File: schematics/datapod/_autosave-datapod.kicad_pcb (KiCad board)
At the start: 2 copper layers, 152.7 x 152.7 mm, 61 parts, among them J1 Conn_01x02, J2 Conn_02x03_Odd_Even, J3 Conn_01x02, J4 DB9_Female, J5 DB9_Male_MountingHoles, J6 Micro_SD_Card, J7 Conn_02x02_Odd_Even, J8 Conn_01x02_Female, K1 DS2E-SL2-DC5V, K2 DS2E-SL2-DC5V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

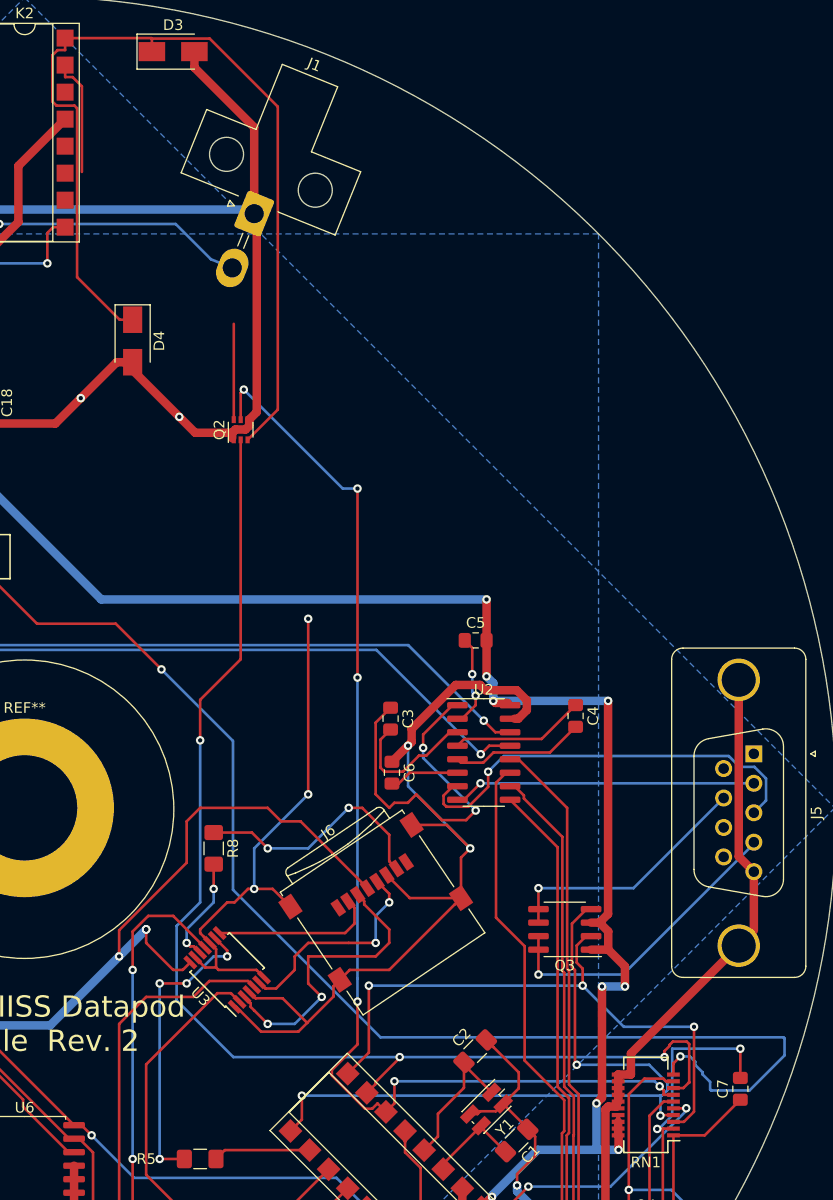
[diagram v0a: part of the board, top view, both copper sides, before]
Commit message: added 3d models that somehow were lost.
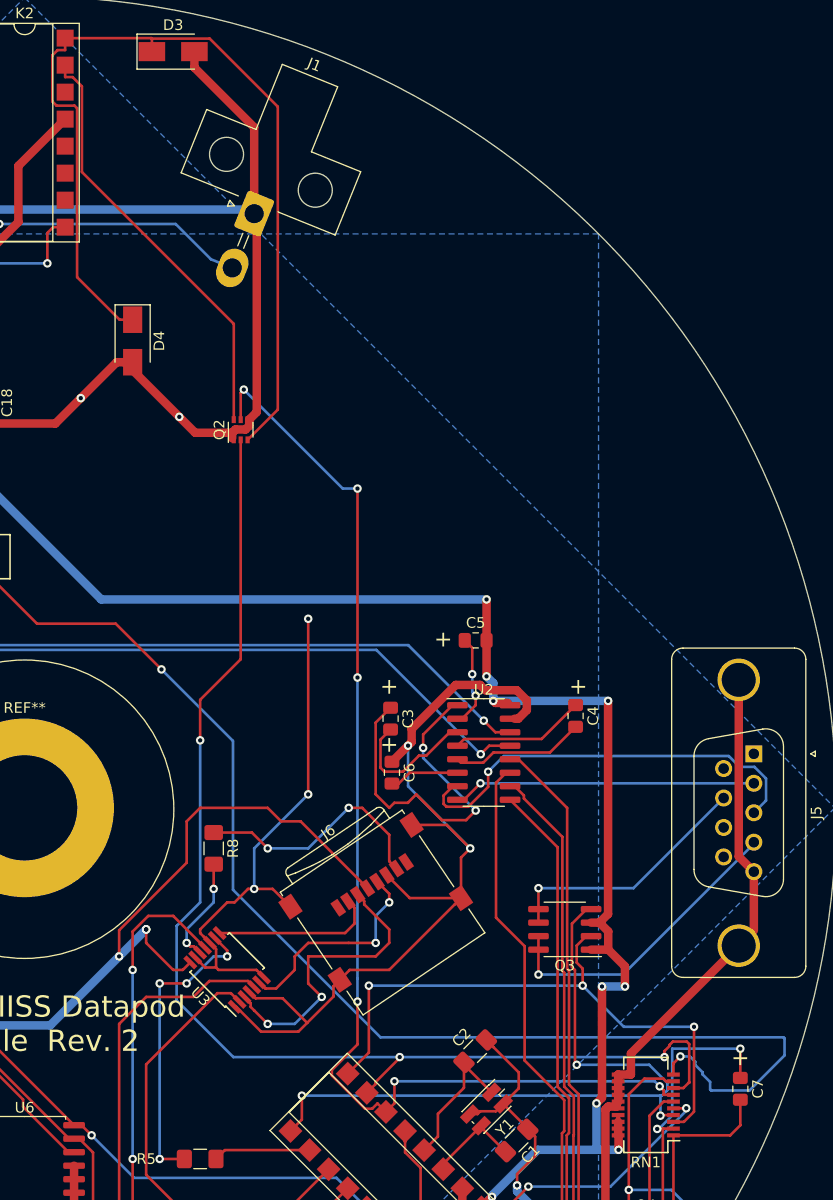
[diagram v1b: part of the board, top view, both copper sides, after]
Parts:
- turned C7 to 270 degrees
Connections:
- C7 pad 1: ~RESET -> DRAIN_PROG
- C7 pad 2: DRAIN_PROG -> ~RESET
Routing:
- net Net-(K2-Pad15): track 20.1 -> 40.3 mm
- net ~RESET: track 28.2 -> 29.6 mm
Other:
- board text added: "+"
